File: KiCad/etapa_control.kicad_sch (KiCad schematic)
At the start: 26 parts, among them J1 DE9_Pins, J2 DE9_Pins, J3 Conn_01x05, SW3 SW_Push_Dual, U20 PIC24HJ128GP502, U3 SN65HVD230, U4 MAX3232, Y1 Crystal

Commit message: Correccions dels sheets i títols fetes
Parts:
- added D3, D4: LED, LED_THT:LED_D3.0mm, symbol Device:LED
- added R6, R7: 10k, Resistor_SMD:R_0805_2012Metric, symbol Device:R
- added R8, R9: 220, Resistor_SMD:R_0805_2012Metric, symbol Device:R
- added SW4, SW5: SW_Push, Button_Switch_SMD:SW_DIP_SPSTx01_Slide_Copal_CHS-01B_W7.62mm_P1.27mm, symbol Switch:SW_Push
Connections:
- net +3.3V: now also R6.1, R7.1
- net DO_control_bomba: now also R8.1
- net DO_control_tancament: now also R9.1
- net GND: now also D3.1 (K), D4.1 (K), SW4.1, SW5.1
- net PULS_START: now also R6.2, SW4.2
- net PULS_STOP: now also R7.2, SW5.2
- new net: D4.2 (A), R9.2
- new net: D3.2 (A), R8.2
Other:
- note added: "Botonera i LEDs pel funcionament dels motors"
- moved on the sheet: C10, C11, J3, R2, SW3, Y1

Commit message: ALFRED DEGANOS SECOOOOS PLS DADDY ALFRED TE CAMELAMOS
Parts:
- added TP4: Tp_Osc_IN, TestPoint:TestPoint_Keystone_5015_Micro_Mini, symbol Connector:TestPoint
- added TP5: Tp_Osc_OUT, TestPoint:TestPoint_Keystone_5015_Micro_Mini, symbol Connector:TestPoint
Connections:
- net OSC_IN: now also TP4.1
- net OSC_OUT: now also TP5.1
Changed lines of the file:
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@@
 	(wire
 		(pts
+			(xy 154.94 90.17) (xy 158.75 90.17)
+		)
+		(stroke
+			(width 0)
+			(type default)
+		)
+	)
+	(wire
+		(pts
 			(xy 31.75 97.79) (xy 34.29 97.79)
 		)
@@
 	(wire
 		(pts
+			(xy 139.7 90.17) (xy 142.24 90.17)
+		)
+		(stroke
+			(width 0)
+			(type default)
+		)
+	)
+	(wire
+		(pts
 			(xy 163.83 177.8) (xy 163.83 176.53)
 		)
@@
 	)
 	(symbol
+		(lib_id "Connector:TestPoint")
+		(at 139.7 90.17 90)
+		(unit 1)
+		(exclude_from_sim no)
+		(in_bom yes)
+		(on_board yes)
+		(dnp no)
+		(fields_autoplaced yes)
+		(property "Reference" "TP4"
+			(at 136.398 85.09 90)
+			(effects
+				(font
+					(size 1.27 1.27)
+				)
+			)
+		)
+		(property "Value" "Tp_Osc_IN"
+			(at 136.398 87.63 90)
+			(effects
+				(font
+					(size 1.27 1.27)
+				)
+			)
+		)
+		(property "Footprint" "TestPoint:TestPoint_Keystone_5015_Micro_Mini"
+			(at 139.7 85.09 0)
+			(effects
+				(font
+					(size 1.27 1.27)
+				)
+				(hide yes)
+			)
+		)
+		(property "Datasheet" "~"
+			(at 139.7 85.09 0)
+			(effects
+				(font
+					(size 1.27 1.27)
+				)
+				(hide yes)
+			)
+		)
+		(property "Description" "test point"
+			(at 139.7 90.17 0)
+			(effects
+				(font
+					(size 1.27 1.27)
+				)
+				(hide yes)
+			)
+		)
+		(pin "1"
+		)
+		(instances
+			(project ""
+				(path "/27a7fca5-115a-450a-aa60-496c314f6c0e/c7bfedf3-33ba-455f-a470-83e81ef64913"
+					(reference "TP4")
+					(unit 1)
+				)
+			)
+		)
+	)
+	(symbol
 		(lib_id "power:+3.3V")
 		(at 172.72 44.45 0)
@@
 					(unit 1)
 				)
+			)
+		)
+	)
+	(symbol
+		(lib_id "Connector:TestPoint")
+		(at 158.75 90.17 270)
+		(unit 1)
+		(exclude_from_sim no)
+		(in_bom yes)
+		(on_board yes)
+		(dnp no)
+		(fields_autoplaced yes)
+		(property "Reference" "TP5"
+			(at 163.83 88.8999 90)
+			(effects
+				(font
+					(size 1.27 1.27)
+				)
+				(justify left)
+			)
+		)
+		(property "Value" "Tp_Osc_OUT"
+			(at 163.83 91.4399 90)
+			(effects
+				(font
+					(size 1.27 1.27)
+				)
+				(justify left)
+			)
+		)
+		(property "Footprint" "TestPoint:TestPoint_Keystone_5015_Micro_Mini"
+			(at 158.75 95.25 0)
+			(effects
+				(font
+					(size 1.27 1.27)
+				)
+				(hide yes)
+			)
+		)
+		(property "Datasheet" "~"
+			(at 158.75 95.25 0)
+			(effects
+				(font
+					(size 1.27 1.27)
+				)
+				(hide yes)
+			)
+		)
+		(property "Description" "test point"
+			(at 158.75 90.17 0)
+			(effects
+				(font
+					(size 1.27 1.27)
+				)
+				(hide yes)
+			)
+		)
+		(pin "1"
+		)
+		(instances
+			(project "PROJECTE_CASTRO_RIBAS"
+				(path "/27a7fca5-115a-450a-aa60-496c314f6c0e/c7bfedf3-33ba-455f-a470-83e81ef64913"
+					(reference "TP5")
+					(unit 1)
+				)

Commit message: ADEUUU
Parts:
- removed TP5: Tp_Osc_OUT, TestPoint:TestPoint_Keystone_5015_Micro_Mini, symbol Connector:TestPoint
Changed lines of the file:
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@@
 	(wire
 		(pts
-			(xy 154.94 90.17) (xy 158.75 90.17)
-		)
-		(stroke
-			(width 0)
-			(type default)
-		)
-	)
-	(wire
-		(pts
 			(xy 31.75 97.79) (xy 34.29 97.79)
 		)
@@
 					(unit 1)
 				)
-			)
-		)
-	)
-	(symbol
-		(lib_id "Connector:TestPoint")
-		(at 158.75 90.17 270)
-		(unit 1)
-		(exclude_from_sim no)
-		(in_bom yes)
-		(on_board yes)
-		(dnp no)
-		(fields_autoplaced yes)
-		(property "Reference" "TP5"
-			(at 163.83 88.8999 90)
-			(effects
-				(font
-					(size 1.27 1.27)
-				)
-				(justify left)
-			)
-		)
-		(property "Value" "Tp_Osc_OUT"
-			(at 163.83 91.4399 90)
-			(effects
-				(font
-					(size 1.27 1.27)
-				)
-				(justify left)
-			)
-		)
-		(property "Footprint" "TestPoint:TestPoint_Keystone_5015_Micro_Mini"
-			(at 158.75 95.25 0)
-			(effects
-				(font
-					(size 1.27 1.27)
-				)
-				(hide yes)
-			)
-		)
-		(property "Datasheet" "~"
-			(at 158.75 95.25 0)
-			(effects
-				(font
-					(size 1.27 1.27)
-				)
-				(hide yes)
-			)
-		)
-		(property "Description" "test point"
-			(at 158.75 90.17 0)
-			(effects
-				(font
-					(size 1.27 1.27)
-				)
-				(hide yes)
-			)
-		)
-		(pin "1"
-		)
-		(instances
-			(project "PROJECTE_CASTRO_RIBAS"
-				(path "/27a7fca5-115a-450a-aa60-496c314f6c0e/c7bfedf3-33ba-455f-a470-83e81ef64913"
-					(reference "TP5")
-					(unit 1)
-				)

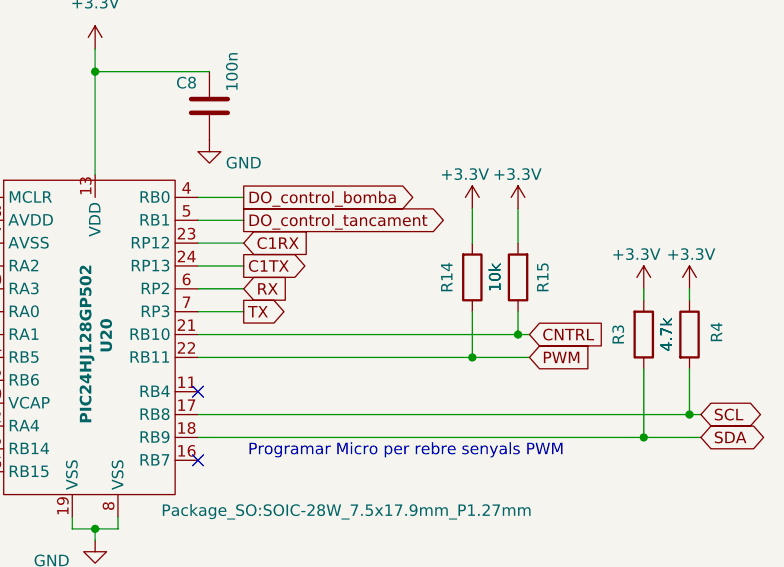
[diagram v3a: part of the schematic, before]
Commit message: Pin del micro pel modul RF triat
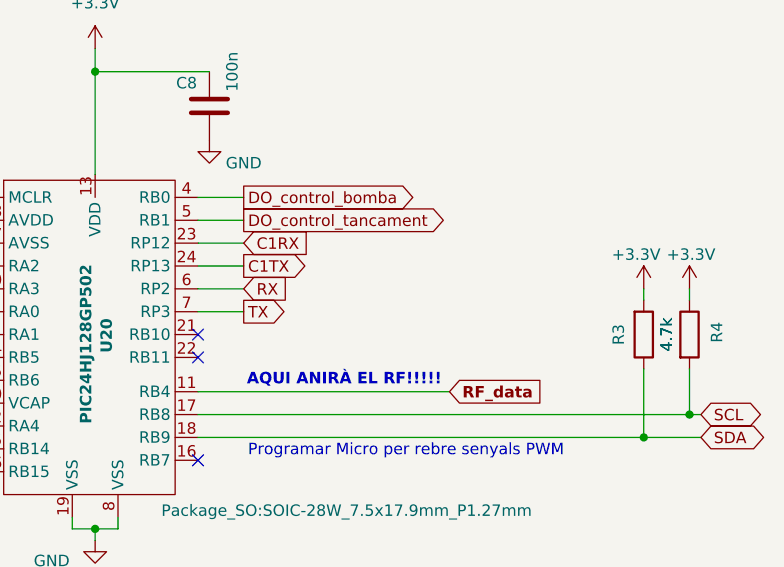
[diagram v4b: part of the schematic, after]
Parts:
- removed R14, R15: 10k, Resistor_SMD:R_0805_2012Metric, symbol Device:R
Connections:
- net RF_data: now reaches U20.11 (RB4)
- net CNTRL: no longer names the net of U20.21 (RB10)
- net PWM: no longer names the net of U20.22 (RB11)
- no-connect marks 22 -> 23
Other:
- note added: "AQUI ANIRÀ EL RF!!!!!"

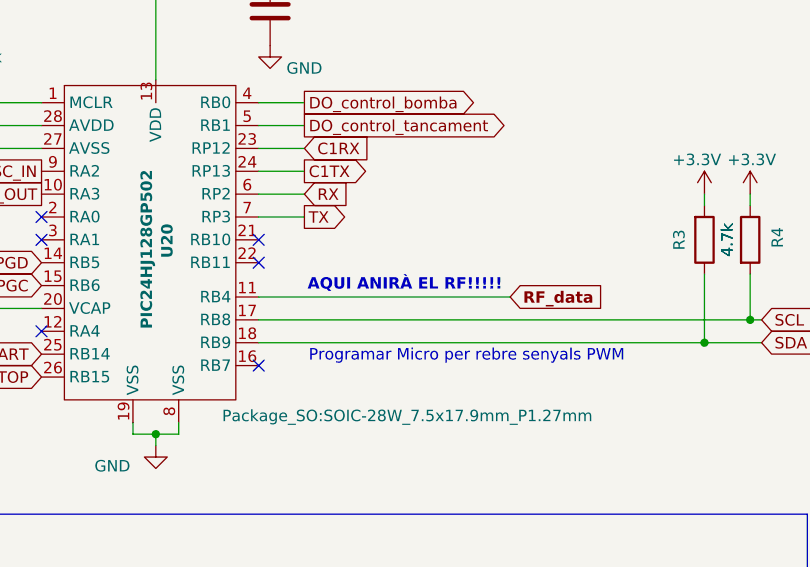
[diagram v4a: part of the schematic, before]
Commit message: Routing de l'alimentació fet, s'ha afegit connector del mòdul RF i plànols millorats
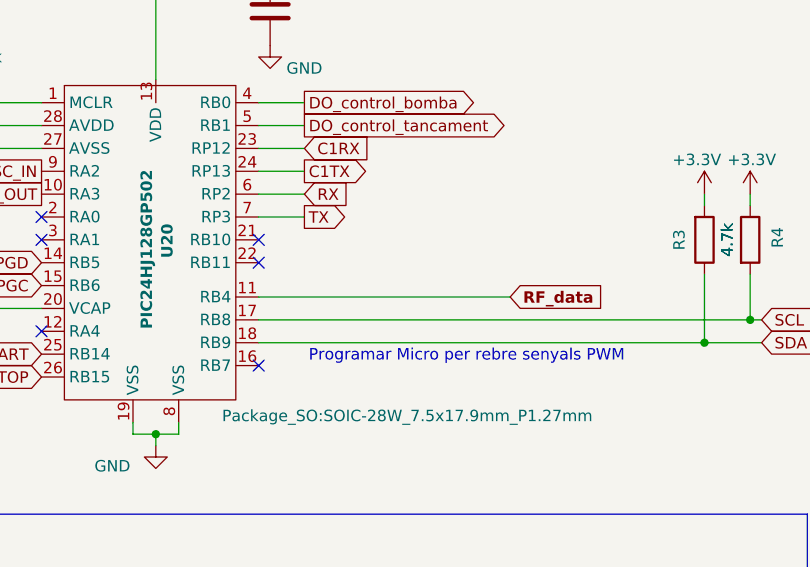
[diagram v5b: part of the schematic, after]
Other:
- note removed: "AQUI ANIRÀ EL RF!!!!!"
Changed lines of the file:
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@@
-		)
-	)
-	(text "AQUI ANIRÀ EL RF!!!!!"
-		(exclude_from_sim no)
-		(at 238.506 62.23 0)
-		(effects
-			(font
-				(size 1.27 1.27)
-				(thickness 0.254)
-				(bold yes)
-			)
 		)
 	)

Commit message: Nose broderk
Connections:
- net RF_data1: now reaches U20.16 (RB7)
- net RF_data renamed RF_data0
- no-connect marks 23 -> 22
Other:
- note removed: "Programar Micro per rebre senyals PWM"
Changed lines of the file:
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@@
 		(comment 1 "Versió 1 de l'esquemàtic de l'etapa de control")
-	)
-	(text "Programar Micro per rebre senyals PWM"
-		(exclude_from_sim no)
-		(at 245.364 70.104 0)
-		(effects
-			(font
-				(size 1.27 1.27)
-			)
-		)
 	)
 	(text "Transceptor CAN\n(equivalent al TJA1050)"
@@
 	)
 	(no_connect
-		(at 222.25 71.12)
-	)
-	(no_connect
 		(at 31.75 55.88)
 	)
@@
 		(pts
 			(xy 96.52 58.42) (xy 96.52 60.96)
+		)
+		(stroke
+			(width 0)
+			(type default)
+		)
+	)
+	(wire
+		(pts
+			(xy 222.25 71.12) (xy 250.19 71.12)
 		)
 		(stroke
@@
 		)
 	)
+	(global_label "RF_data1"
+		(shape input)
+		(at 250.19 71.12 0)
+		(fields_autoplaced yes)
+		(effects
+			(font
+				(size 1.27 1.27)
+			)
+			(justify left)
+		)
+		(property "Intersheetrefs" "${INTERSHEET_REFS}"
+			(at 261.8836 71.12 0)
+			(effects
+				(font
+					(size 1.27 1.27)
+				)
+				(justify left)
+				(hide yes)
+			)
+		)
+	)
 	(global_label "C1RX"
 		(shape output)
@@
 		)
 	)
-	(global_label "RF_data"
+	(global_label "RF_data0"
 		(shape input)
 		(at 250.19 63.5 0)
@@
 			(font
 				(size 1.27 1.27)
-				(thickness 0.254)
-				(bold yes)
+				(thickness 0.1588)
 			)
 			(justify left)
 		)
 		(property "Intersheetrefs" "${INTERSHEET_REFS}"
-			(at 261.1501 63.5 0)
-			(effects
-				(font
+			(at 261.8836 63.5 0)
+			(effects
+				(font

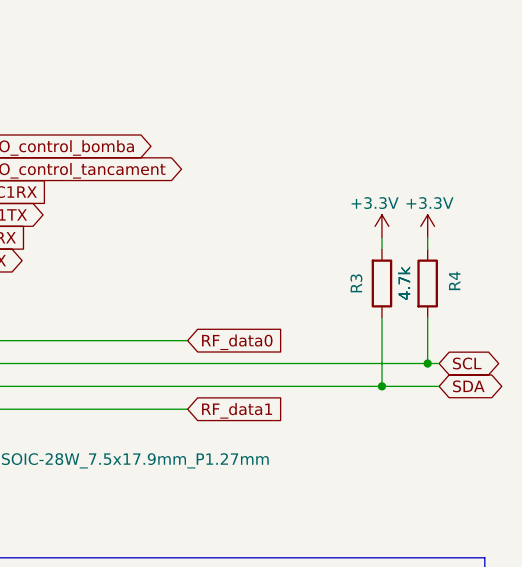
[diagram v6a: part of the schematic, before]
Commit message: Algunes correccions del professor (esquemàtic i pcb)
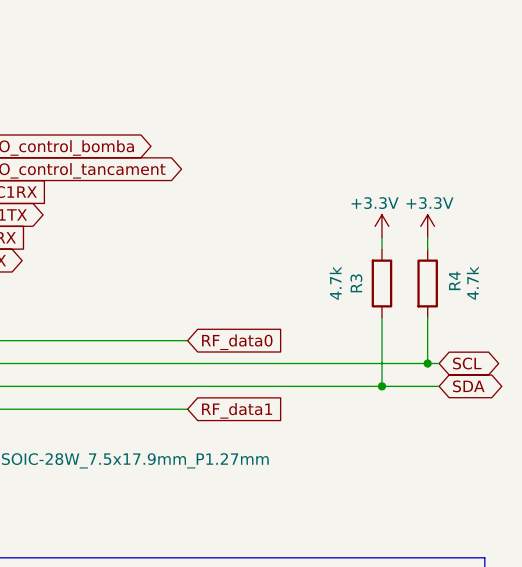
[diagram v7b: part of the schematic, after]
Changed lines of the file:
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@@
 		)
 		(property "Value" "4.7k"
-			(at 274.32 57.15 90)
+			(at 266.7 57.15 90)
 			(effects
 				(font
@@
 		)
 		(property "Value" "4.7k"
-			(at 274.32 57.15 90)
-			(effects
-				(font
+			(at 281.94 57.15 90)
+			(effects
+				(font
